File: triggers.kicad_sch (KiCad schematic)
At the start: 20 parts, among them U10 SN74LVC2G17DB, U11 SN74LVC2G17DB, U13 SRV05-4, U9 SN74LVC2G17DB

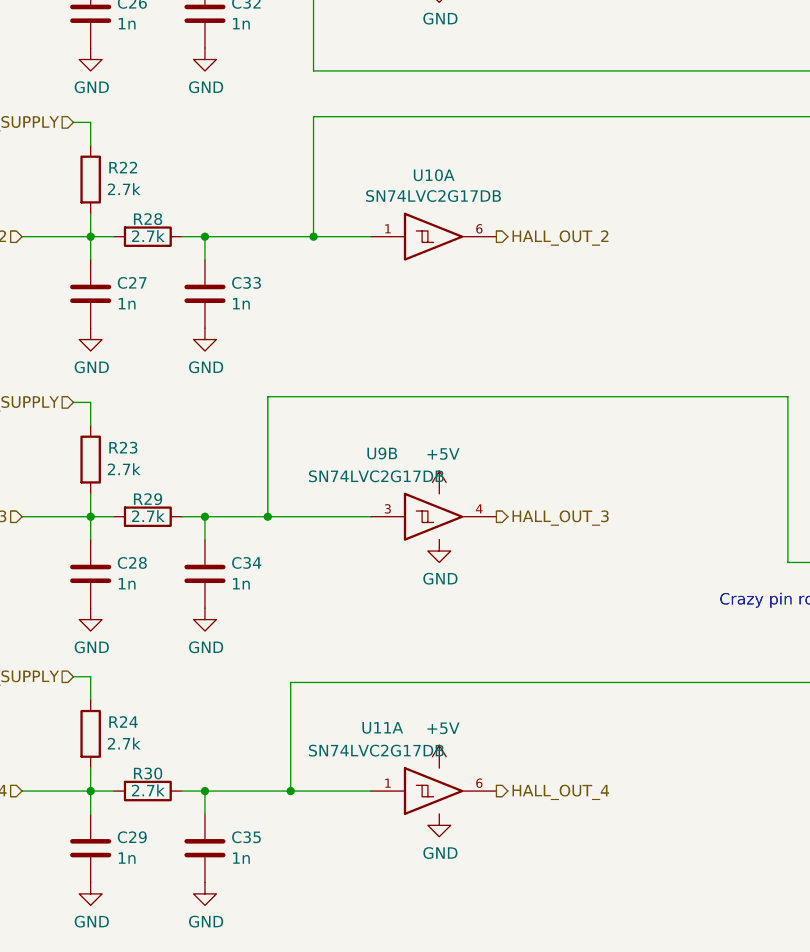
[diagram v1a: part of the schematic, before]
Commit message: Add power LEDs, silkscreen beautifying, remove U11 use U10B
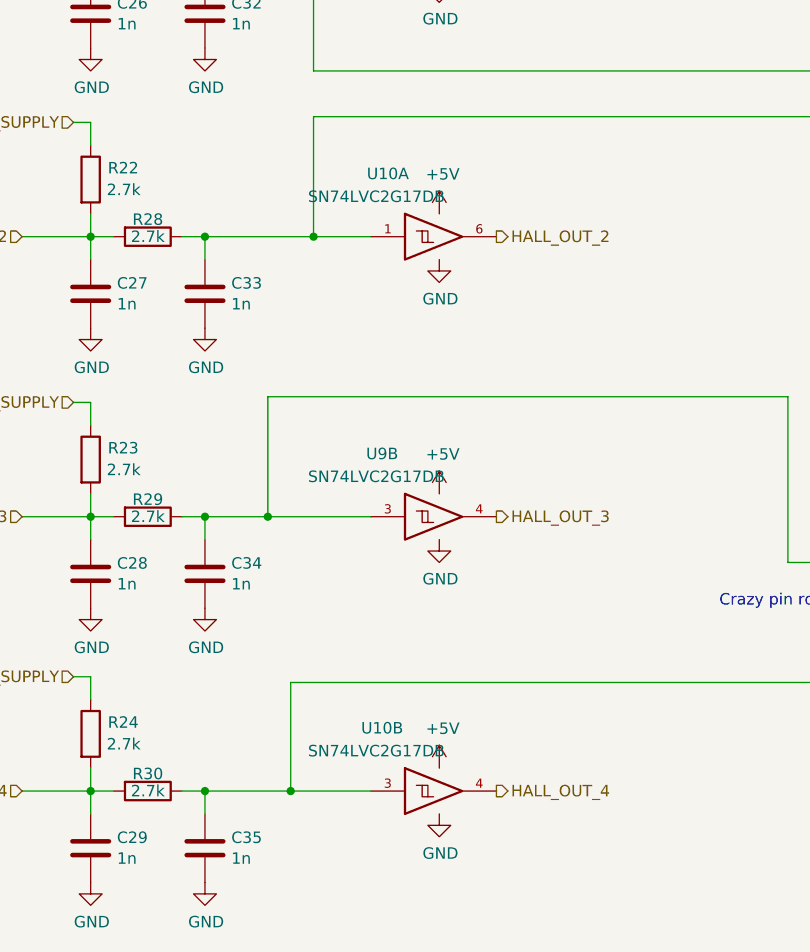
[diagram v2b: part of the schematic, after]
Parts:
- removed U11: SN74LVC2G17DB, Package_TO_SOT_SMD:SOT-23-6, symbol 74xGxx:74LVC2G17
- added unit 2 of U10
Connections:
- net +5V: now also U10.5 (VCC)
- net GND: now also U10.2 (GND)
- net HALL_OUT_4: now also U10.4
- net at C35.1, R30.1, U13.1 (IO1): now also U10.3
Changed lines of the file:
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@@
   (symbol (lib_id "74xGxx:74LVC2G17") (at 76.2 59.055 0) (unit 1)
     (in_bom yes) (on_board yes) (dnp no)
-    (property "Reference" "U10" (at 75.565 52.2732 0)
-      (effects (font (size 1.27 1.27)))
-    )
-    (property "Value" "SN74LVC2G17DB" (at 75.565 54.5846 0)
+    (property "Reference" "U10" (at 70.485 52.07 0)
+      (effects (font (size 1.27 1.27)))
+    )
+    (property "Value" "SN74LVC2G17DB" (at 69.215 54.61 0)
       (effects (font (size 1.27 1.27)))
     )
@@
         (path "/d9116601-cae2-4199-827b-70fa136aae51/00000000-0000-0000-0000-00005dd8090b"
           (reference "#PWR076") (unit 1)
-        )
-      )
-    )
-  )
-  (symbol (lib_id "74xGxx:74LVC2G17") (at 76.2 120.65 0) (unit 1)
-    (in_bom yes) (on_board yes) (dnp no)
-    (property "Reference" "U11" (at 69.85 113.665 0)
-      (effects (font (size 1.27 1.27)))
-    )
-    (property "Value" "SN74LVC2G17DB" (at 69.215 116.205 0)
-      (effects (font (size 1.27 1.27)))
-    )
-    (property "Footprint" "Package_TO_SOT_SMD:SOT-23-6" (at 76.2 120.65 0)
-      (effects (font (size 1.27 1.27)) hide)
-    )
-    (property "Datasheet" "http://www.ti.com/lit/sg/scyt129e/scyt129e.pdf" (at 76.2 120.65 0)
-      (effects (font (size 1.27 1.27)) hide)
-    )
-    (property "LCSC" "C10429" (at 76.2 120.65 0)
-      (effects (font (size 1.27 1.27)) hide)
-    )
-    (property "LCSC_ext" "1" (at 76.2 120.65 0)
-      (effects (font (size 1.27 1.27)) hide)
-    )
-    (property "PN" "74HC2G17GW" (at 76.2 120.65 0)
-      (effects (font (size 1.27 1.27)) hide)
-    )
-    (pin "2")
-    (pin "5")
-    (pin "1")
-    (pin "6")
-    (pin "3")
-    (pin "4")
-    (instances
-      (project "proteus"
-        (path "/d9116601-cae2-4199-827b-70fa136aae51/00000000-0000-0000-0000-00005dd8090b"
-          (reference "U11") (unit 1)
         )
       )
@@
         )
       )
+    )
+  )
+  (symbol (lib_id "power:+5V") (at 76.2 56.515 0) (unit 1)
+    (in_bom yes) (on_board yes) (dnp no)
+    (property "Reference" "#PWR091" (at 76.2 60.325 0)
+      (effects (font (size 1.27 1.27)) hide)
+    )
+    (property "Value" "+5V" (at 76.581 52.1208 0)
+      (effects (font (size 1.27 1.27)))
+    )
+    (property "Footprint" "" (at 76.2 56.515 0)
+      (effects (font (size 1.27 1.27)) hide)
+    )
+    (property "Datasheet" "" (at 76.2 56.515 0)
+      (effects (font (size 1.27 1.27)) hide)
+    )
+    (pin "1")
+    (instances
+      (project "proteus"
+        (path "/d9116601-cae2-4199-827b-70fa136aae51/00000000-0000-0000-0000-00005dd8090b"
+          (reference "#PWR091") (unit 1)
+        )
+      )
+    )
+  )
+  (symbol (lib_id "74xGxx:74LVC2G17") (at 76.2 120.65 0) (unit 2)
+    (in_bom yes) (on_board yes) (dnp no)
+    (property "Reference" "U10" (at 69.85 113.665 0)
+      (effects (font (size 1.27 1.27)))
+    )
+    (property "Value" "SN74LVC2G17DB" (at 69.215 116.205 0)
+      (effects (font (size 1.27 1.27)))
+    )
+    (property "Footprint" "Package_TO_SOT_SMD:SOT-23-6" (at 76.2 120.65 0)
+      (effects (font (size 1.27 1.27)) hide)
+    )
+    (property "Datasheet" "http://www.ti.com/lit/sg/scyt129e/scyt129e.pdf" (at 76.2 120.65 0)
+      (effects (font (size 1.27 1.27)) hide)
+    )
+    (property "LCSC" "C10429" (at 76.2 120.65 0)
+      (effects (font (size 1.27 1.27)) hide)
+    )
+    (property "LCSC_ext" "1" (at 76.2 120.65 0)
+      (effects (font (size 1.27 1.27)) hide)
+    )
+    (property "PN" "74HC2G17GW" (at 76.2 120.65 0)
+      (effects (font (size 1.27 1.27)) hide)
+    )
+    (pin "2")
+    (pin "5")
+    (pin "1")
+    (pin "6")
+    (pin "3")
+    (pin "4")
+    (instances
+      (project "proteus"
+        (path "/d9116601-cae2-4199-827b-70fa136aae51/00000000-0000-0000-0000-00005dd8090b"
+          (reference "U10") (unit 2)
+        )
+      )
+    )
+  )
+  (symbol (lib_id "power:GND") (at 76.2 61.595 0) (unit 1)
+    (in_bom yes) (on_board yes) (dnp no)
+    (property "Reference" "#PWR092" (at 76.2 67.945 0)
+      (effects (font (size 1.27 1.27)) hide)
+    )
+    (property "Value" "GND" (at 76.327 65.9892 0)
+      (effects (font (size 1.27 1.27)))
+    )
+    (property "Footprint" "" (at 76.2 61.595 0)
+      (effects (font (size 1.27 1.27)) hide)
+    )
+    (property "Datasheet" "" (at 76.2 61.595 0)
+      (effects (font (size 1.27 1.27)) hide)
+    )
+    (pin "1")
+    (instances
+      (project "proteus"
+        (path "/d9116601-cae2-4199-827b-70fa136aae51/00000000-0000-0000-0000-00005dd8090b"
+          (reference "#PWR092") (unit 1)
+        )
+      )

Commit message: Several optimizations
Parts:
- added C37, C38, C39, C40: 1n, Capacitor_SMD:C_0603_1608Metric, symbol Device:C
- added C43: 100n, Capacitor_SMD:C_0603_1608Metric, symbol Device:C
- added R132, R133, R134, R135: 2.7k, Resistor_SMD:R_0603_1608Metric, symbol Device:R
- added U14: SN74LVC2G17DB, Package_TO_SOT_SMD:SOT-23-6, symbol 74xGxx:74LVC2G17
- added U15: SRV05-4, Package_TO_SOT_SMD:SOT-23-6, symbol Power_Protection:SRV05-4
- added U28: 74HC14, SOIC-14_3.9x8.7mm_P1.27mm, symbol 74xx:74HC14
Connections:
- net +5V: now also C43.2, U14.5 (VCC), U14.5 (VCC), U15.5 (VP), U28.14 (VCC)
- net 5V_SENSOR_SUPPLY: now also R132.1, R133.1
- net GND: now also C37.2, C38.2, C39.2, C40.2, C43.1, U14.2 (GND), U14.2 (GND), U15.2 (VN), U28.7 (GND)
- net HALL_OUT_1: now also U28.8
- net HALL_OUT_2: now also U28.4
- net HALL_OUT_3: now also U28.6
- net HALL_OUT_4: now also U28.2
- net Schmitt_In_1: now reaches C32.1, R27.1, U13.3 (IO2), U9.1
- net Schmitt_In_1: now also U28.9
- net Schmitt_In_2: now reaches C33.1, R28.1, U10.1, U13.4 (IO3)
- net Schmitt_In_2: now also U28.3
- net Schmitt_In_3: now reaches C34.1, R29.1, U13.6 (IO4), U9.3
- net Schmitt_In_3: now also U28.5
- net Schmitt_In_4: now reaches C35.1, R30.1, U10.3, U13.1 (IO1)
- net Schmitt_In_4: now also U28.1
- new net HALL_IN_5: C37.1, R132.2, R134.2
- new net HALL_IN_6: C38.1, R133.2, R135.2
- new net HALL_OUT_5: U14.6, U28.10
- new net HALL_OUT_6: U14.4, U28.12
- new net Schmitt_In_5: C39.1, R134.1, U14.1, U15.3 (IO2), U28.11
- new net Schmitt_In_6: C40.1, R135.1, U14.3, U15.1 (IO1), U28.13
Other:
- note removed: "Crazy pin routing is to make PCB layout simpler"
- moved on the sheet: U10A, U10B, U13, U9A, U9B

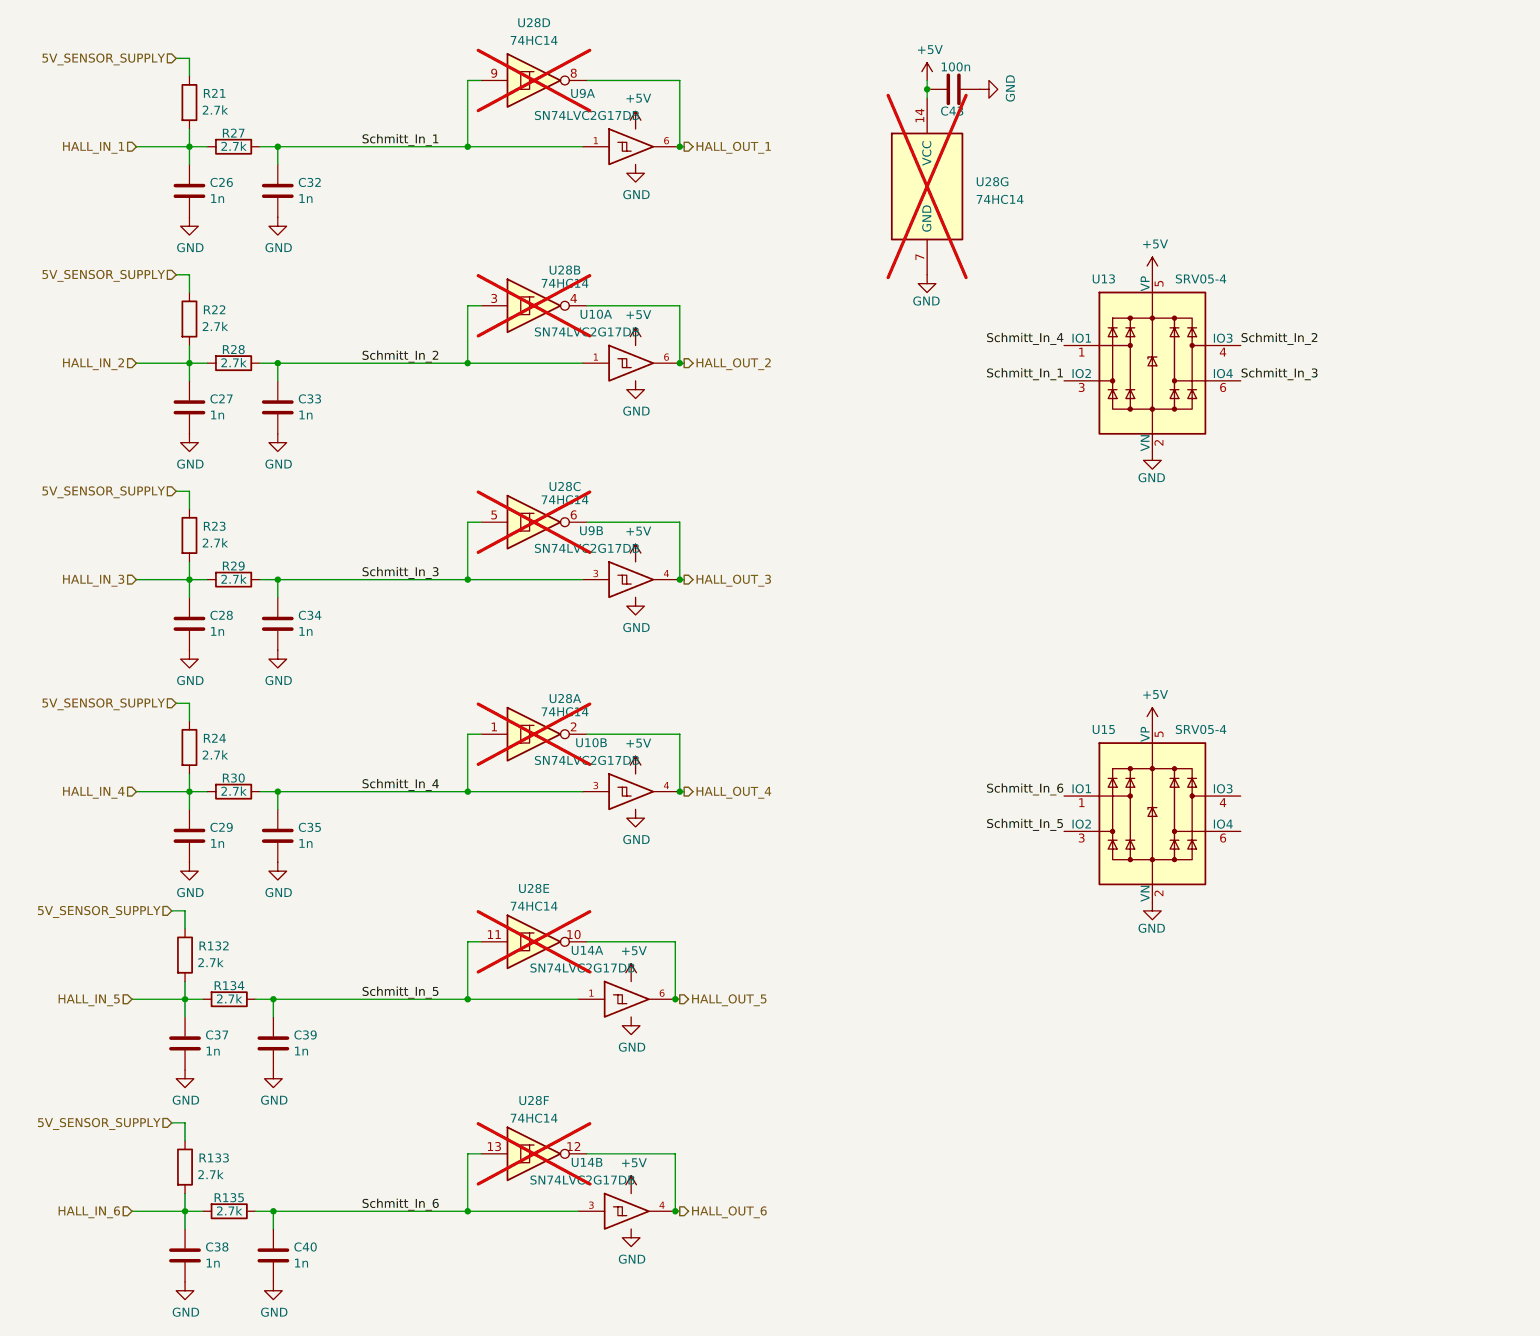
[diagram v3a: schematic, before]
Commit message: Add Stepper, fix Connector, add Testpoints, several changes
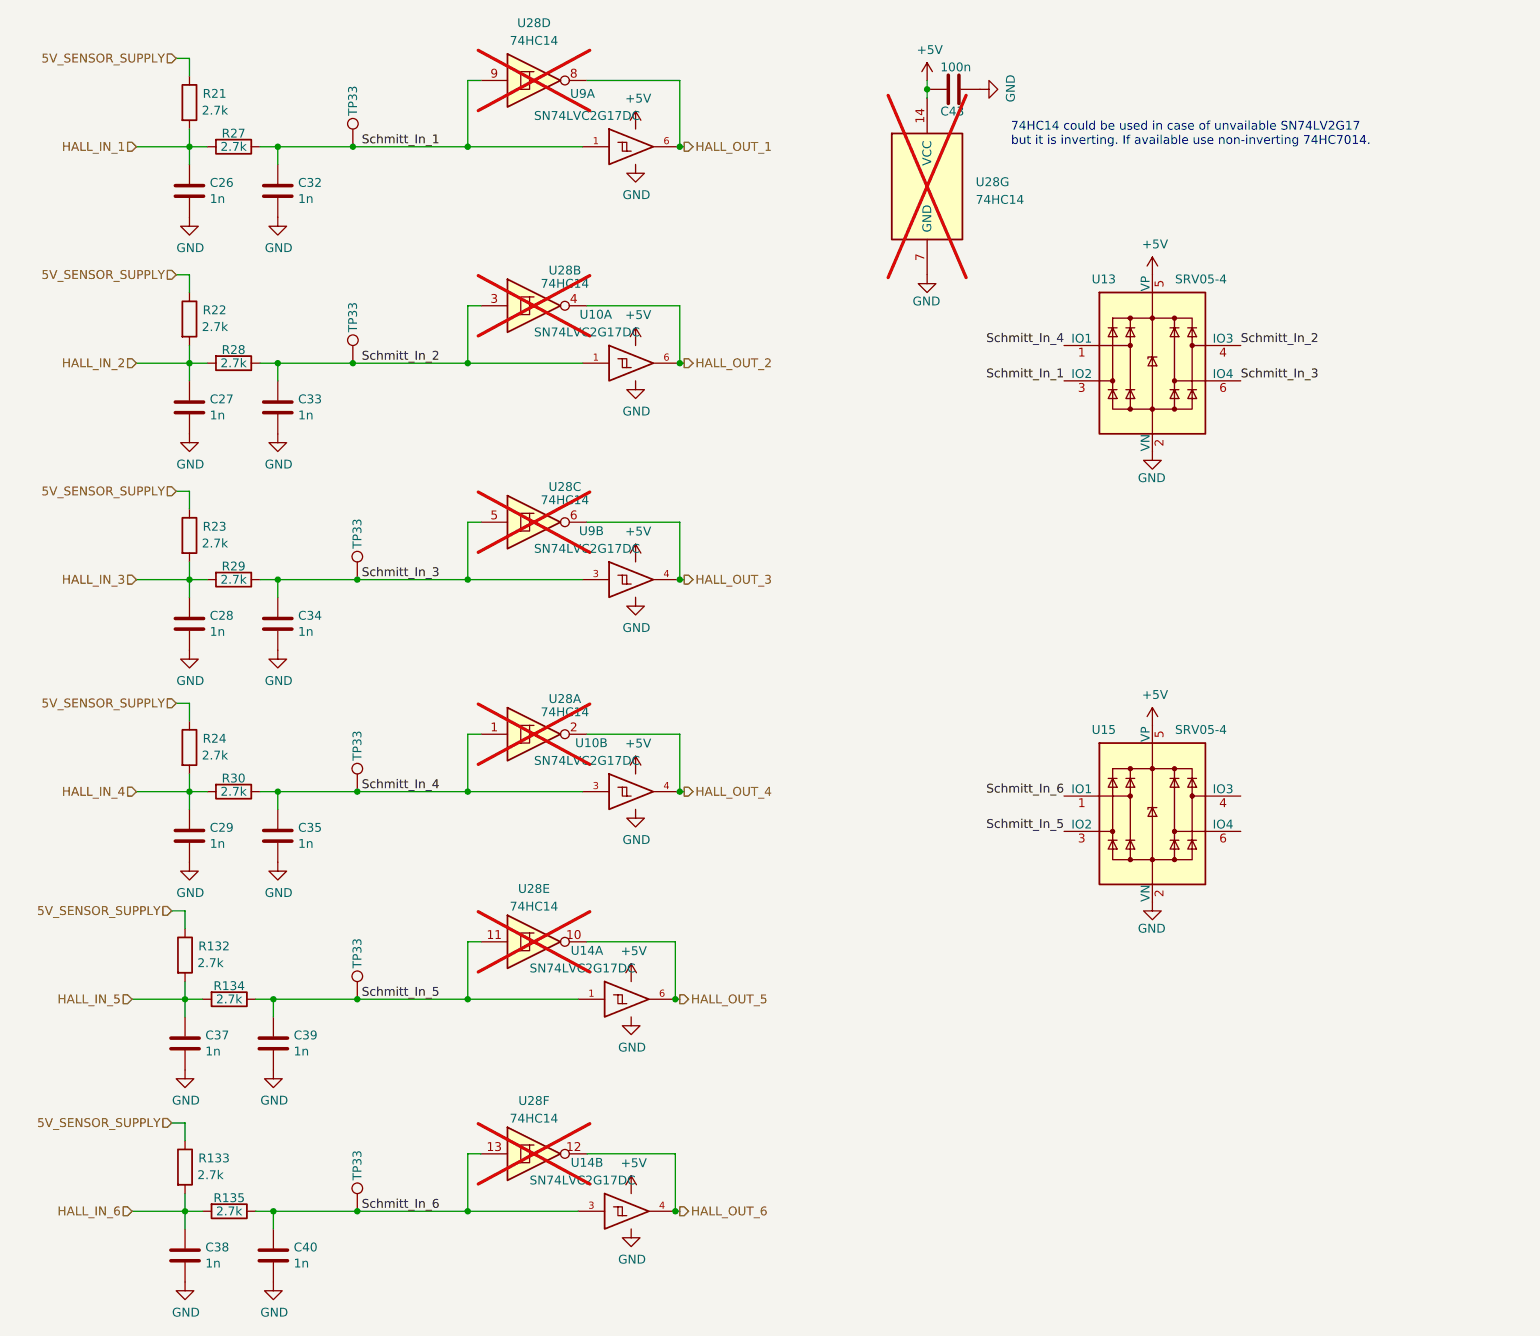
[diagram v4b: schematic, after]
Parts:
- added TP33 (x6): TestPoint, TestPoint:TestPoint_Pad_D1.0mm, symbol Connector:TestPoint
- U10, U14, U9: value SN74LVC2G17DB -> SN74LVC2G17DC; footprint Package_TO_SOT_SMD:SOT-23-6 -> Package_TO_SOT_SMD:SOT-363_SC-70-6; LCSC C10429 -> C50714; PN 74HC2G17GW -> (none)
- U28: now left out of the parts list
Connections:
- net Schmitt_In_1: now also TP33.1
- net Schmitt_In_2: now also TP33.1
- net Schmitt_In_3: now also TP33.1
- net Schmitt_In_4: now also TP33.1
- net Schmitt_In_5: now also TP33.1
- net Schmitt_In_6: now also TP33.1
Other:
- note added: "74HC14 could be used in case of unvailable SN74LV2G17 but it is inverting. If available use non-inverting 74HC7014."

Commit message: Optimize
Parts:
- U13, U15: LCSC (none) -> C85364
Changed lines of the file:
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@@
+      (effects (font (size 1.27 1.27)) hide)
+    )
+    (property "LCSC" "C85364" (at 175.895 59.055 0)
       (effects (font (size 1.27 1.27)) hide)
     )
@@
       (effects (font (size 1.27 1.27)) hide)
     )
+    (property "LCSC" "C85364" (at 175.895 123.825 0)
+      (effects (font (size 1.27 1.27)) hide)
+    )
